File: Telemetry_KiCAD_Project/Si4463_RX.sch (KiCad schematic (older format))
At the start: 14 parts, among them U2 Si4463, Y1 30MHz

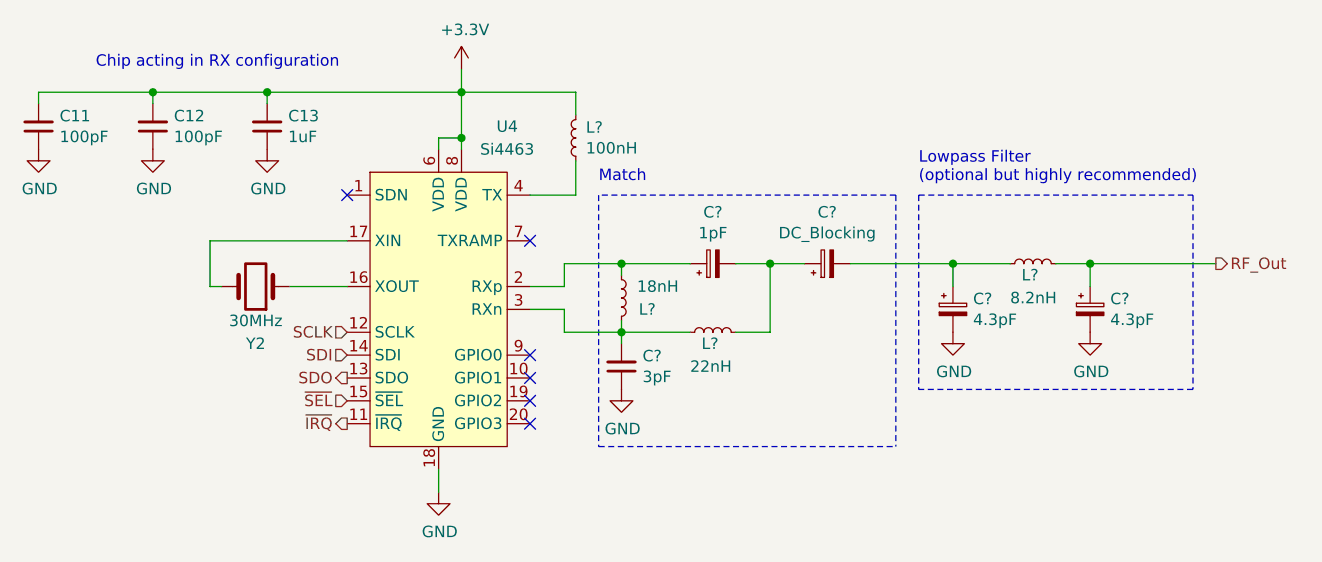
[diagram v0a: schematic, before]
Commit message: Added TX/RX matching network passives to PCB
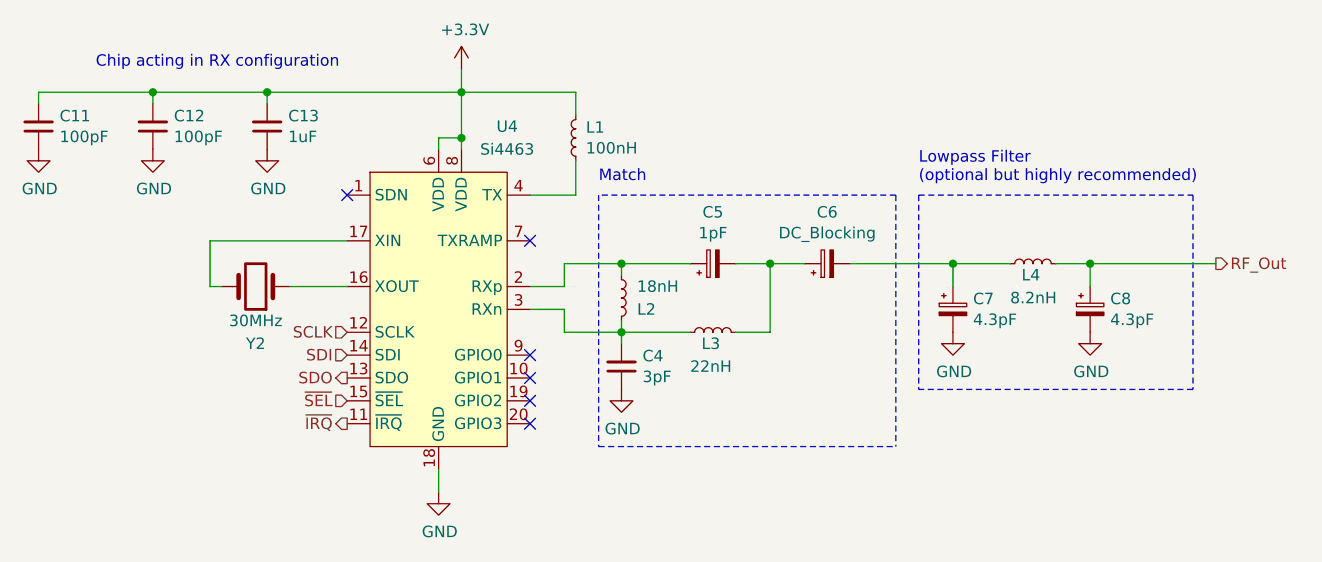
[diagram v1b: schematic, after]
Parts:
- removed L?: 100nH, symbol Device:L_Small
- added L1: 100nH, Inductor_SMD:L_0603_1608Metric, symbol Device:L_Small
- C5, C6, C7, C8: renamed from C?; footprint (none) -> Capacitor_SMD:C_0603_1608Metric
- L2, L3, L4: renamed from L?; footprint (none) -> Inductor_SMD:L_0603_1608Metric
- gave numbers to parts that had none: 1
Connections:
- net +3V3: now also L1.2
- net at U2.4 (TX): now also L1.1
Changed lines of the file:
@@
 $EndDescr
-$Comp
-L RF:Si4463 U2
-U 1 1 619D9E16
-P 6150 3650
-AR Path="/619D9C89/619D9E16" Ref="U2"  Part="1"
-AR Path="/61A0416A/619D9E16" Ref="U4"  Part="1"
-F 0 "U4" H 6450 4450 50  0000 C CNN
-F 1 "Si4463" H 6450 4350 50  0000 C CNN
-F 2 "Package_DFN_QFN:QFN-20-1EP_4x4mm_P0.5mm_EP2.6x2.6mm_ThermalVias" H 6150 4850 50  0001 C CNN
-F 3 "https://www.silabs.com/documents/public/data-sheets/Si4464-63-61-60.pdf" H 5850 3550 50  0001 C CNN
-F 4 "https://www.silabs.com/content/usergenerated/asi/cloud/attachments/siliconlabs/en/community/wireless/bluetooth/forum/jcr:content/content/primary/qna/tune_an_rf_pico_boar-pg5F/AN648_Si4X6X%20AND%20EZR32%20HIGH-POWER%20PA%20MATCHING.pdf" H 6150 3650 50  0001 C CNN "Matching Guide"
-	1    6150 3650
-	1    0    0    -1
-$EndComp
 $Comp
 L power:GND #PWR0104
@@
 $Comp
 L power:+3.3V #PWR0105
-U 1 1 619DB460
+U 1 1 61AFA3CB
 P 6250 2600
-AR Path="/619D9C89/619DB460" Ref="#PWR0105"  Part="1"
-AR Path="/61A0416A/619DB460" Ref="#PWR0117"  Part="1"
+AR Path="/619D9C89/61AFA3CB" Ref="#PWR0105"  Part="1"
+AR Path="/61A0416A/61AFA3CB" Ref="#PWR0117"  Part="1"
 F 0 "#PWR0117" H 6250 2450 50  0001 C CNN
 F 1 "+3.3V" H 6265 2773 50  0000 C CNN
@@
 $Comp
 L Device:Crystal Y1
-U 1 1 619DAC0C
+U 1 1 61AFA3C9
 P 5350 3550
-AR Path="/619D9C89/619DAC0C" Ref="Y1"  Part="1"
-AR Path="/61A0416A/619DAC0C" Ref="Y2"  Part="1"
+AR Path="/619D9C89/61AFA3C9" Ref="Y1"  Part="1"
+AR Path="/61A0416A/61AFA3C9" Ref="Y2"  Part="1"
 F 0 "Y2" H 5350 3800 50  0000 C CNN
 F 1 "30MHz" H 5350 3700 50  0000 C CNN
@@
 $Comp
 L power:GND #PWR0110
-U 1 1 619F9A7C
+U 1 1 61AFA3D0
 P 4900 2950
-AR Path="/619D9C89/619F9A7C" Ref="#PWR0110"  Part="1"
-AR Path="/61A0416A/619F9A7C" Ref="#PWR0122"  Part="1"
+AR Path="/619D9C89/61AFA3D0" Ref="#PWR0110"  Part="1"
+AR Path="/61A0416A/61AFA3D0" Ref="#PWR0122"  Part="1"
 F 0 "#PWR0122" H 4900 2700 50  0001 C CNN
 F 1 "GND" H 4905 2777 50  0000 C CNN
@@
 $Comp
 L Device:L_Small L?
-U 1 1 61AC1A40
+U 1 1 61AFA3D2
 P 6750 2900
-AR Path="/619D9C89/61AC1A40" Ref="L?"  Part="1"
-AR Path="/61A0416A/61AC1A40" Ref="L?"  Part="1"
-F 0 "L?" H 6706 2854 50  0000 R CNN
+AR Path="/619D9C89/61AFA3D2" Ref="L?"  Part="1"
+AR Path="/61A0416A/61AFA3D2" Ref="L1"  Part="1"
+F 0 "L1" H 6706 2854 50  0000 R CNN
 F 1 "100nH" H 6706 2945 50  0000 R CNN
-F 2 "" H 6750 2900 50  0001 C CNN
+F 2 "Inductor_SMD:L_0603_1608Metric" H 6750 2900 50  0001 C CNN
 F 3 "~" H 6750 2900 50  0001 C CNN
 	1    6750 2900
@@
 P 6950 3600
 AR Path="/619D9C89/61AD4DA6" Ref="L?"  Part="1"
-AR Path="/61A0416A/61AD4DA6" Ref="L?"  Part="1"
-F 0 "L?" H 7100 3550 50  0000 R CNN
+AR Path="/61A0416A/61AD4DA6" Ref="L2"  Part="1"
+F 0 "L2" H 7100 3550 50  0000 R CNN
 F 1 "18nH" H 7200 3650 50  0000 R CNN
-F 2 "" H 6950 3600 50  0001 C CNN
+F 2 "Inductor_SMD:L_0603_1608Metric" H 6950 3600 50  0001 C CNN
 F 3 "~" H 6950 3600 50  0001 C CNN
 	1    6950 3600
@@
 P 6950 3900
 AR Path="/619D9C89/61AD69A7" Ref="C?"  Part="1"
-AR Path="/61A0416A/61AD69A7" Ref="C?"  Part="1"
-F 0 "C?" H 6858 3854 50  0000 R CNN
+AR Path="/61A0416A/61AD69A7" Ref="C4"  Part="1"
+F 0 "C4" H 6858 3854 50  0000 R CNN
 F 1 "3pF" H 6858 3945 50  0000 R CNN
 F 2 "Capacitor_SMD:C_0603_1608Metric" H 6950 3900 50  0001 C CNN
@@
 P 6950 4000
 AR Path="/619D9C89/61AD75B9" Ref="#PWR?"  Part="1"
-AR Path="/61A0416A/61AD75B9" Ref="#PWR?"  Part="1"
-F 0 "#PWR?" H 6950 3750 50  0001 C CNN
+AR Path="/61A0416A/61AD75B9" Ref="#PWR08"  Part="1"
+F 0 "#PWR08" H 6950 3750 50  0001 C CNN
 F 1 "GND" H 6955 3827 50  0000 C CNN
 F 2 "" H 6950 4000 50  0001 C CNN
@@
 P 7350 3750
 AR Path="/619D9C89/61AD7AF2" Ref="L?"  Part="1"
-AR Path="/61A0416A/61AD7AF2" Ref="L?"  Part="1"
-F 0 "L?" V 7300 3800 50  0000 R CNN
+AR Path="/61A0416A/61AD7AF2" Ref="L3"  Part="1"
+F 0 "L3" V 7300 3800 50  0000 R CNN
 F 1 "22nH" V 7200 3850 50  0000 R CNN
-F 2 "" H 7350 3750 50  0001 C CNN
+F 2 "Inductor_SMD:L_0603_1608Metric" H 7350 3750 50  0001 C CNN
 F 3 "~" H 7350 3750 50  0001 C CNN
 	1    7350 3750
@@
 	7600 3450 7450 3450
 $Comp
-L Device:CP_Small C?
+L Device:CP_Small C5
 U 1 1 61ADAF5B
 P 7350 3450
-F 0 "C?" V 7575 3450 50  0000 C CNN
+F 0 "C5" V 7575 3450 50  0000 C CNN
 F 1 "1pF" V 7484 3450 50  0000 C CNN
-F 2 "" H 7350 3450 50  0001 C CNN
+F 2 "Capacitor_SMD:C_0603_1608Metric" H 7350 3450 50  0001 C CNN
 F 3 "~" H 7350 3450 50  0001 C CNN
 	1    7350 3450
@@
 $EndComp
 $Comp
-L Device:CP_Small C?
+L Device:CP_Small C6
 U 1 1 61ADCBDF
 P 7850 3450
-F 0 "C?" V 8075 3450 50  0000 C CNN
+F 0 "C6" V 8075 3450 50  0000 C CNN
 F 1 "DC_Blocking" V 7984 3450 50  0000 C CNN
-F 2 "" H 7850 3450 50  0001 C CNN
+F 2 "Capacitor_SMD:C_0603_1608Metric" H 7850 3450 50  0001 C CNN
 F 3 "~" H 7850 3450 50  0001 C CNN
 	1    7850 3450
@@
 Connection ~ 7600 3450
 $Comp
-L Device:CP_Small C?
+L Device:CP_Small C7
 U 1 1 61ADE208
 P 8400 3650
-F 0 "C?" H 8488 3696 50  0000 L CNN
+F 0 "C7" H 8488 3696 50  0000 L CNN
 F 1 "4.3pF" H 8488 3605 50  0000 L CNN
-F 2 "" H 8400 3650 50  0001 C CNN
+F 2 "Capacitor_SMD:C_0603_1608Metric" H 8400 3650 50  0001 C CNN
 F 3 "~" H 8400 3650 50  0001 C CNN
 	1    8400 3650
@@
 P 8750 3450
 AR Path="/619D9C89/61ADF4C6" Ref="L?"  Part="1"
-AR Path="/61A0416A/61ADF4C6" Ref="L?"  Part="1"
-F 0 "L?" V 8700 3500 50  0000 R CNN
+AR Path="/61A0416A/61ADF4C6" Ref="L4"  Part="1"
+F 0 "L4" V 8700 3500 50  0000 R CNN
 F 1 "8.2nH" V 8600 3550 50  0000 R CNN
-F 2 "" H 8750 3450 50  0001 C CNN
+F 2 "Inductor_SMD:L_0603_1608Metric" H 8750 3450 50  0001 C CNN
 F 3 "~" H 8750 3450 50  0001 C CNN
 	1    8750 3450
@@
 P 8400 3750
 AR Path="/619D9C89/61AE08E5" Ref="#PWR?"  Part="1"
-AR Path="/61A0416A/61AE08E5" Ref="#PWR?"  Part="1"
-F 0 "#PWR?" H 8400 3500 50  0001 C CNN
+AR Path="/61A0416A/61AE08E5" Ref="#PWR09"  Part="1"
+F 0 "#PWR09" H 8400 3500 50  0001 C CNN
 F 1 "GND" H 8405 3577 50  0000 C CNN
 F 2 "" H 8400 3750 50  0001 C CNN
@@
 $EndComp
 $Comp
-L Device:CP_Small C?
+L Device:CP_Small C8
 U 1 1 61AE0EE4
 P 9000 3650
-F 0 "C?" H 9088 3696 50  0000 L CNN
+F 0 "C8" H 9088 3696 50  0000 L CNN
 F 1 "4.3pF" H 9088 3605 50  0000 L CNN
-F 2 "" H 9000 3650 50  0001 C CNN
+F 2 "Capacitor_SMD:C_0603_1608Metric" H 9000 3650 50  0001 C CNN
 F 3 "~" H 9000 3650 50  0001 C CNN
 	1    9000 3650
@@
 P 9000 3750
 AR Path="/619D9C89/61AE1D40" Ref="#PWR?"  Part="1"
-AR Path="/61A0416A/61AE1D40" Ref="#PWR?"  Part="1"
-F 0 "#PWR?" H 9000 3500 50  0001 C CNN
+AR Path="/61A0416A/61AE1D40" Ref="#PWR010"  Part="1"
+F 0 "#PWR010" H 9000 3500 50  0001 C CNN
 F 1 "GND" H 9005 3577 50  0000 C CNN
 F 2 "" H 9000 3750 50  0001 C CNN
@@
 	6700 3650 6550 3650
 Wire Wire Line
+	6550 3550 6700 3550
+Wire Wire Line
+	6700 3550 6700 3450
+Wire Wire Line
+	6700 3450 6950 3450
+Wire Wire Line
+	6550 3150 6750 3150
+Wire Wire Line
+	6750 3150 6750 3000
+Wire Wire Line
 	6700 3750 6950 3750
-Wire Wire Line
-	6550 3550 6700 3550
-Wire Wire Line
-	6700 3550 6700 3450
-Wire Wire Line
-	6700 3450 6950 3450
-Wire Wire Line
-	6550 3150 6750 3150
-Wire Wire Line
-	6750 3150 6750 3000
+$Comp
+L RF:Si4463 U2
+U 1 1 61AFA3C8
+P 6150 3650
+AR Path="/619D9C89/61AFA3C8" Ref="U2"  Part="1"
+AR Path="/61A0416A/61AFA3C8" Ref="U4"  Part="1"
+F 0 "U4" H 6450 4450 50  0000 C CNN
+F 1 "Si4463" H 6450 4350 50  0000 C CNN
+F 2 "Package_DFN_QFN:QFN-20-1EP_4x4mm_P0.5mm_EP2.6x2.6mm_ThermalVias" H 6150 4850 50  0001 C CNN
+F 3 "https://www.silabs.com/documents/public/data-sheets/Si4464-63-61-60.pdf" H 5850 3550 50  0001 C CNN
+F 4 "https://www.silabs.com/content/usergenerated/asi/cloud/attachments/siliconlabs/en/community/wireless/bluetooth/forum/jcr:content/content/primary/qna/tune_an_rf_pico_boar-pg5F/AN648_Si4X6X%20AND%20EZR32%20HIGH-POWER%20PA%20MATCHING.pdf" H 6150 3650 50  0001 C CNN "Matching Guide"
+	1    6150 3650
+	1    0    0    -1
+$EndComp
 $EndSCHEMATC

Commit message: Added RSD Duplexer Footprint, rearranged RF matching networks
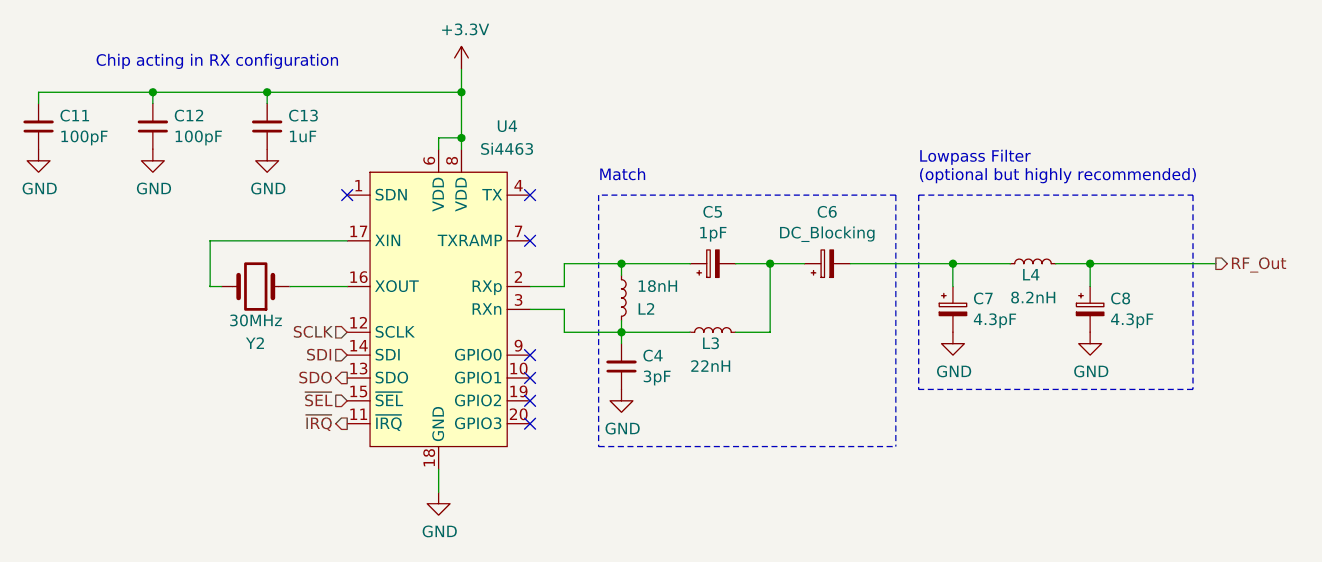
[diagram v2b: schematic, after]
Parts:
- removed L1: 100nH, Inductor_SMD:L_0603_1608Metric, symbol Device:L_Small
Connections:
- no-connect marks 6 -> 7
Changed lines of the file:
@@
 NoConn ~ 6550 3350
 NoConn ~ 5750 3150
-$Comp
-L Device:L_Small L?
-U 1 1 61AFA3D2
-P 6750 2900
-AR Path="/619D9C89/61AFA3D2" Ref="L?"  Part="1"
-AR Path="/61A0416A/61AFA3D2" Ref="L1"  Part="1"
-F 0 "L1" H 6706 2854 50  0000 R CNN
-F 1 "100nH" H 6706 2945 50  0000 R CNN
-F 2 "Inductor_SMD:L_0603_1608Metric" H 6750 2900 50  0001 C CNN
-F 3 "~" H 6750 2900 50  0001 C CNN
-	1    6750 2900
-	-1   0    0    1
-$EndComp
-Wire Wire Line
-	6750 2800 6750 2700
-Wire Wire Line
-	6750 2700 6250 2700
 Text HLabel 9550 3450 2    50   Output ~ 0
 RF_Out
@@
 	6700 3450 6950 3450
 Wire Wire Line
-	6550 3150 6750 3150
-Wire Wire Line
-	6750 3150 6750 3000
-Wire Wire Line
 	6700 3750 6950 3750
 $Comp
@@
 	1    0    0    -1
 $EndComp
+NoConn ~ 6550 3150
 $EndSCHEMATC
